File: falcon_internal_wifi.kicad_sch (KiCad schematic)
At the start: 16 parts, among them J1 Conn_01x05, U1 LM1117-3.3, U2 ESP-12F, U3 NC7ST04M5X

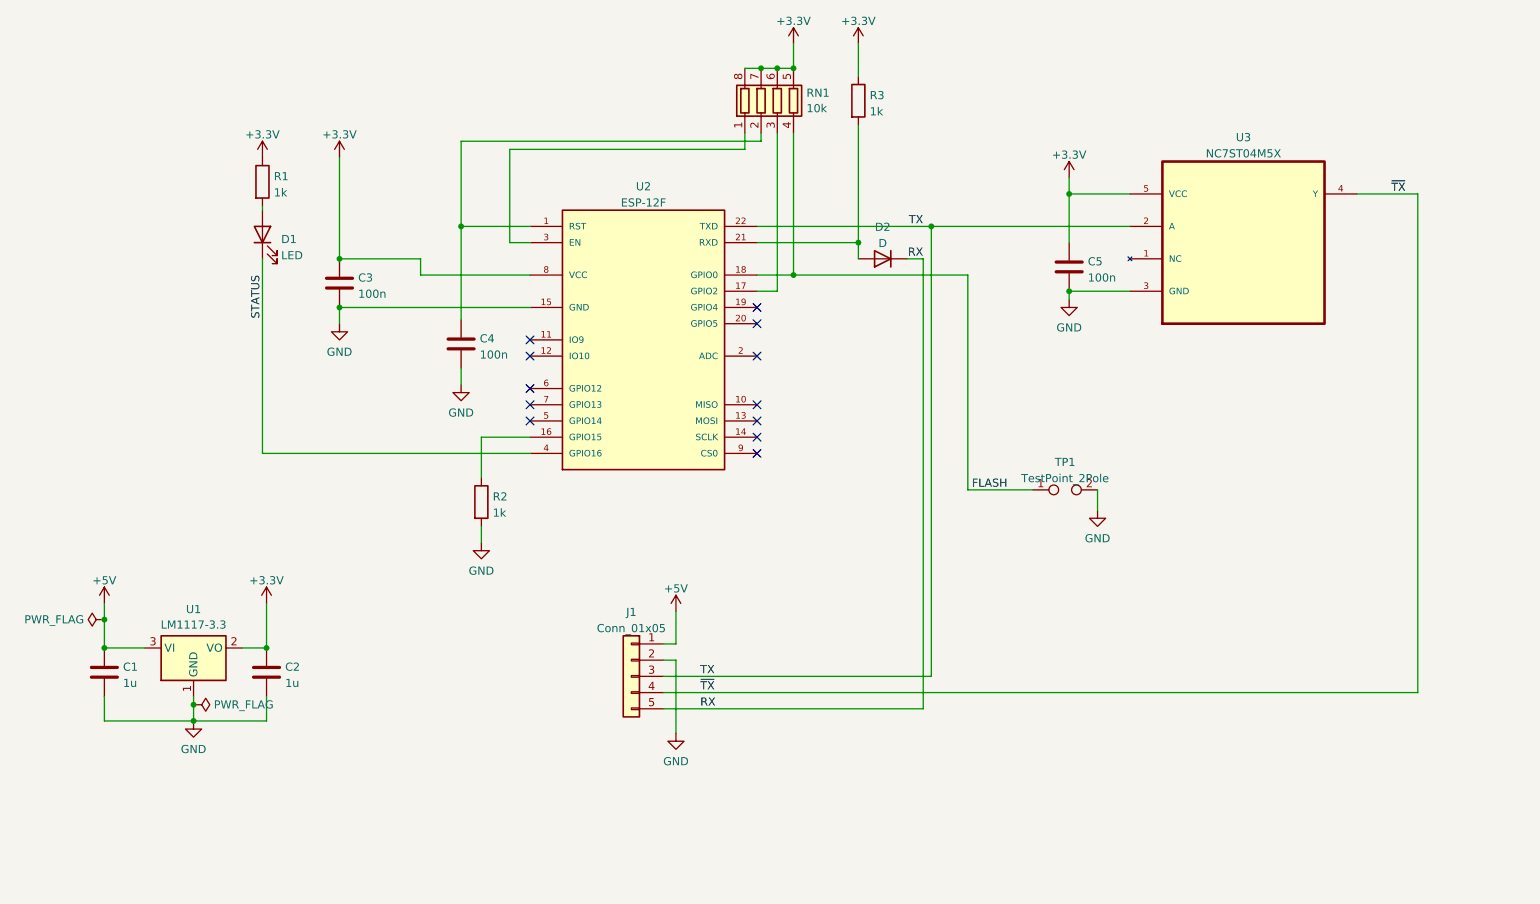
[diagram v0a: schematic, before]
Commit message: Second design with smaller passive
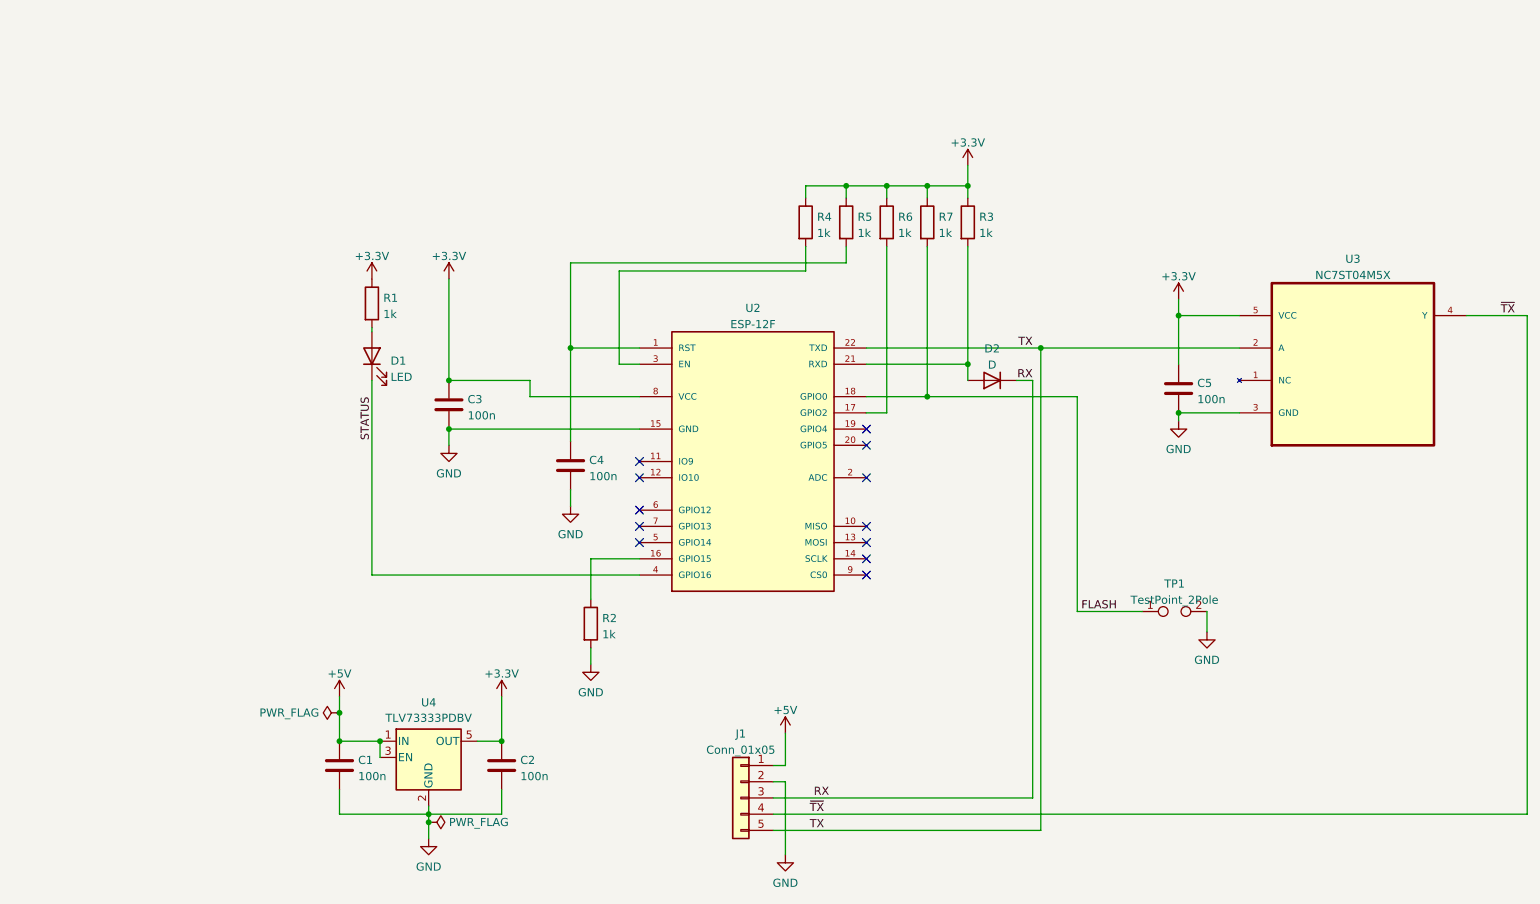
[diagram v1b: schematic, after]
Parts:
- removed RN1: 10k, Resistor_SMD:R_Array_Convex_4x0612, symbol Device:R_Pack04
- removed U1: LM1117-3.3, Package_TO_SOT_SMD:SOT-223-3_TabPin2, symbol Regulator_Linear:AMS1117-3.3
- added R4, R5, R6, R7: 1k, Resistor_SMD:R_0603_1608Metric, symbol Device:R
- added U4: TLV73333PDBV, Package_TO_SOT_SMD:SOT-23-5, symbol Regulator_Linear:TLV73333PDBV
- C1, C2: value 1u -> 100n; footprint Capacitor_SMD:C_0805_2012Metric -> Capacitor_SMD:C_0603_1608Metric
- C3, C4, C5: footprint Capacitor_SMD:C_0805_2012Metric -> Capacitor_SMD:C_0603_1608Metric
- R1, R2, R3: footprint Resistor_SMD:R_0805_2012Metric -> Resistor_SMD:R_0603_1608Metric
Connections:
- net +3.3V: now also R4.1, R5.1, R6.1, R7.1, U4.5 (OUT)
- net +5V: now also U4.1 (IN), U4.3 (EN)
- net FLASH: now also R7.2
- net GND: now also U4.2 (GND)
- net RX: now also J1.3 (Pin_3); no longer J1.5 (Pin_5)
- net TX: now also J1.5 (Pin_5); no longer J1.3 (Pin_3)
- net at C4.1, U2.1 (RST): now also R5.2
- net at U2.17 (GPIO2): now also R6.2
- net at U2.3 (EN): now also R4.2
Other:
- moved on the sheet: C1, C2, C3, C4, C5, D1, D2, J1, R1, R2, R3, TP1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
